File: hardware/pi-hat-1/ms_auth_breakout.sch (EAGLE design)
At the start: 28 parts, among them IC1 ULN2003AD, J11 BUCK_MODULEHORIZONTAL, J9 POWER_JACKPTH_LOCK, Q1 DMN3023L, Q2 DMN3023L, Q3 DMN3023L, Q4 DMN3023L

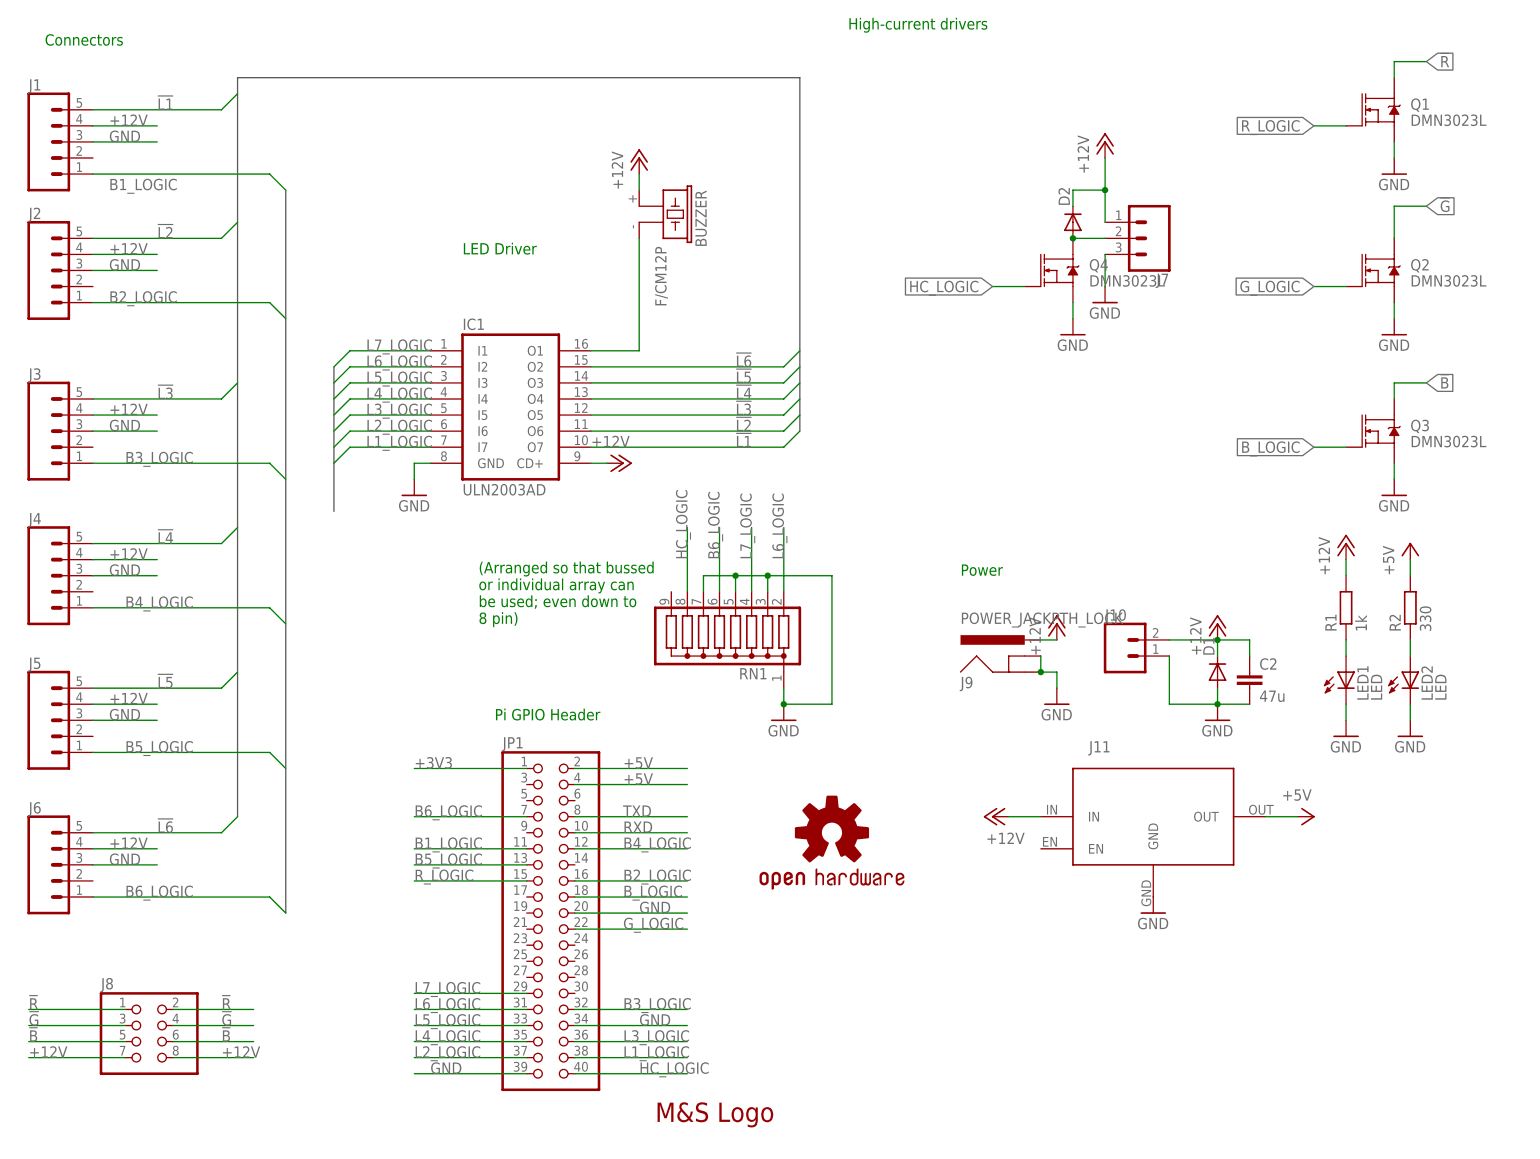
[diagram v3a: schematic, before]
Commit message: Rework board to add two relays.
Also remove buzzer, change LED connector, and standardize on smaller
freewheel diodes.  Not quire ready for 0.4 cut; needs airwires routed
for relays with solder jumpers.
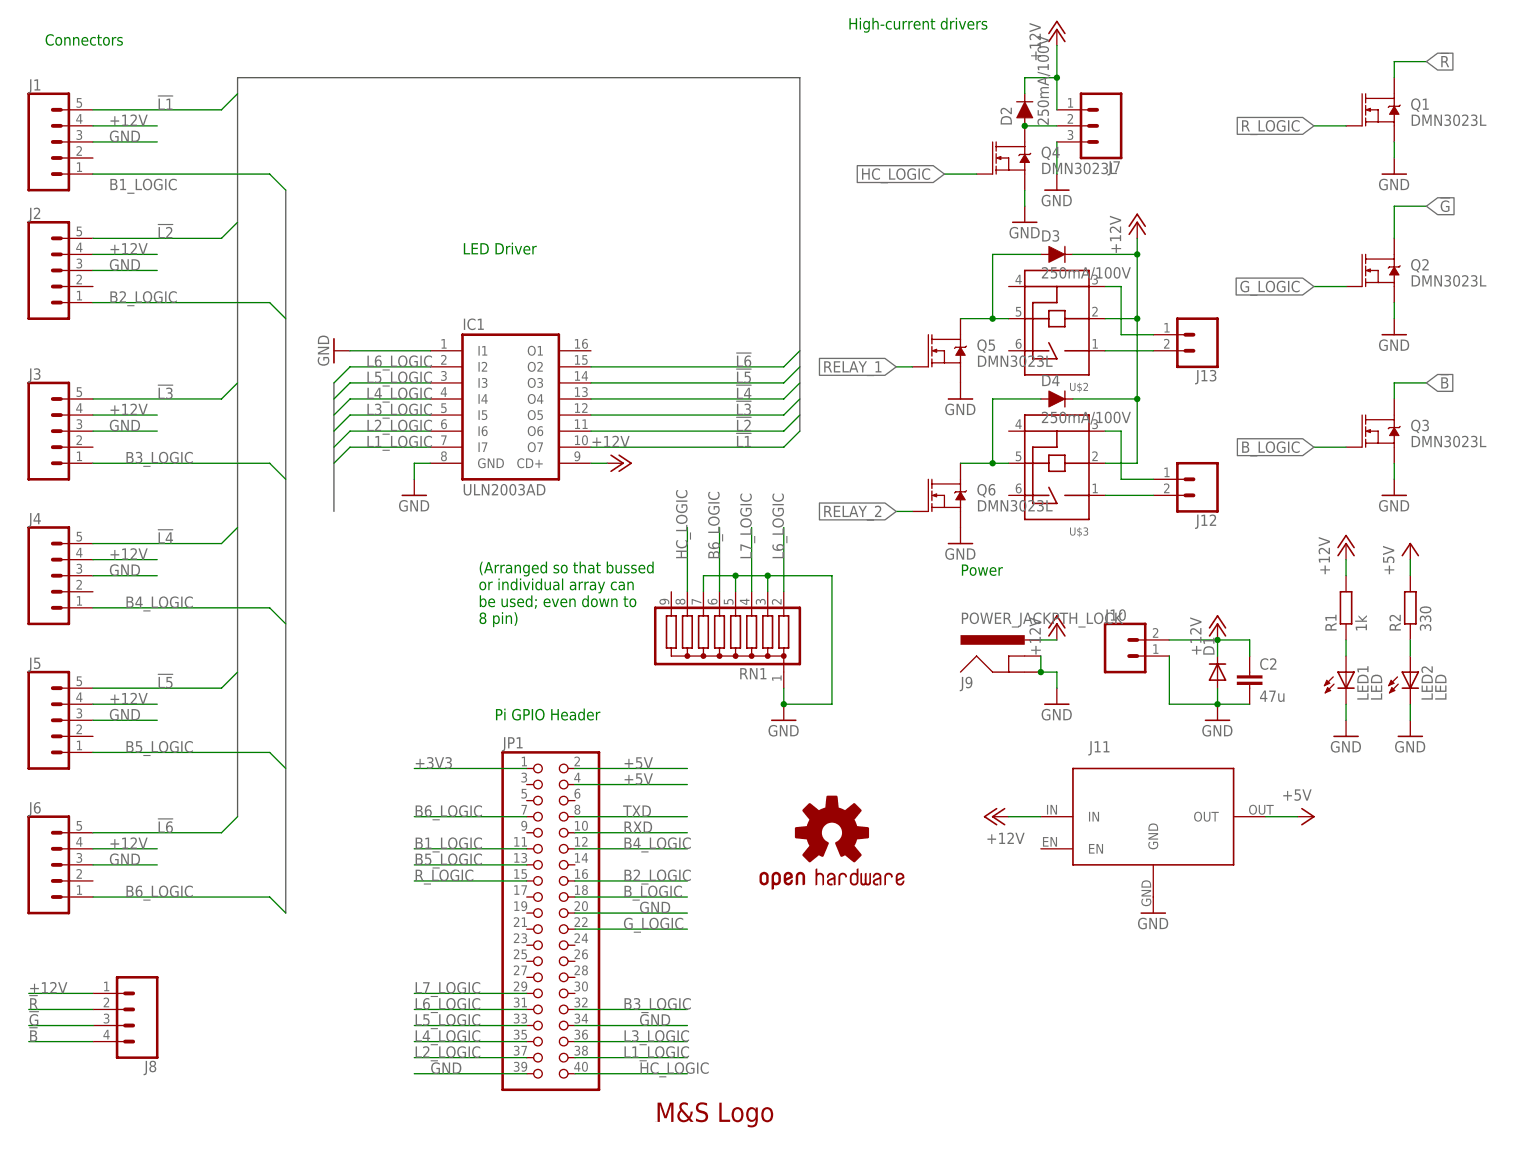
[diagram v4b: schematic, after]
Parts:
- removed BUZZER: F/CM12P, buzzer:F/CM12P
- added D3, D4: 250mA/100V, SparkFun-DiscreteSemi:DIODE-BAS16J
- added J12, J13: (no value), SparkFun-Connectors:CONN_02POLAR_LOCK
- added Q5, Q6: DMN3023L, SparkFun-DiscreteSemi:MOSFET-NCH-AO3404A
- added U$2, U$3: HFD23_SPDT, hfd23:HFD23_SPDT
- D2: value (none) -> 250mA/100V; device diode:DIODE-DO-214AC -> SparkFun-DiscreteSemi:DIODE-BAS16J
- J8: device pinhead:PINHD-2X4 -> SparkFun-Connectors:CONN_04POLAR_LOCK
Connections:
- removed net N$13: BUZZER.2, IC1.O1
- new net N$10: J13.1, U$2.3
- new net N$12: J12.1, U$3.3
- new net N$14: J12.2, U$3.1
- new net N$2: D4.A, Q6.D, U$3.5
- new net N$5: D3.A, Q5.D, U$2.5
- new net N$9: J13.2, U$2.1
- new net RELAY_1: Q5.G
- new net RELAY_2: Q6.G
- net !B: now also J8.4; no longer J8.5, J8.6
- net !G: no longer J8.4
- net !R: no longer J8.1
- net +12V: now also D3.C, D4.C, J8.1, U$2.2, U$3.2; no longer BUZZER.1, J8.7, J8.8
- net GND: now also IC1.I1, Q5.S, Q6.S
- net L7_LOGIC: no longer IC1.I1
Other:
- moved on the sheet: J7, Q4

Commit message: pi-hat-1 v0.4 as-ordered
(Forgot to route the relay connections though.)
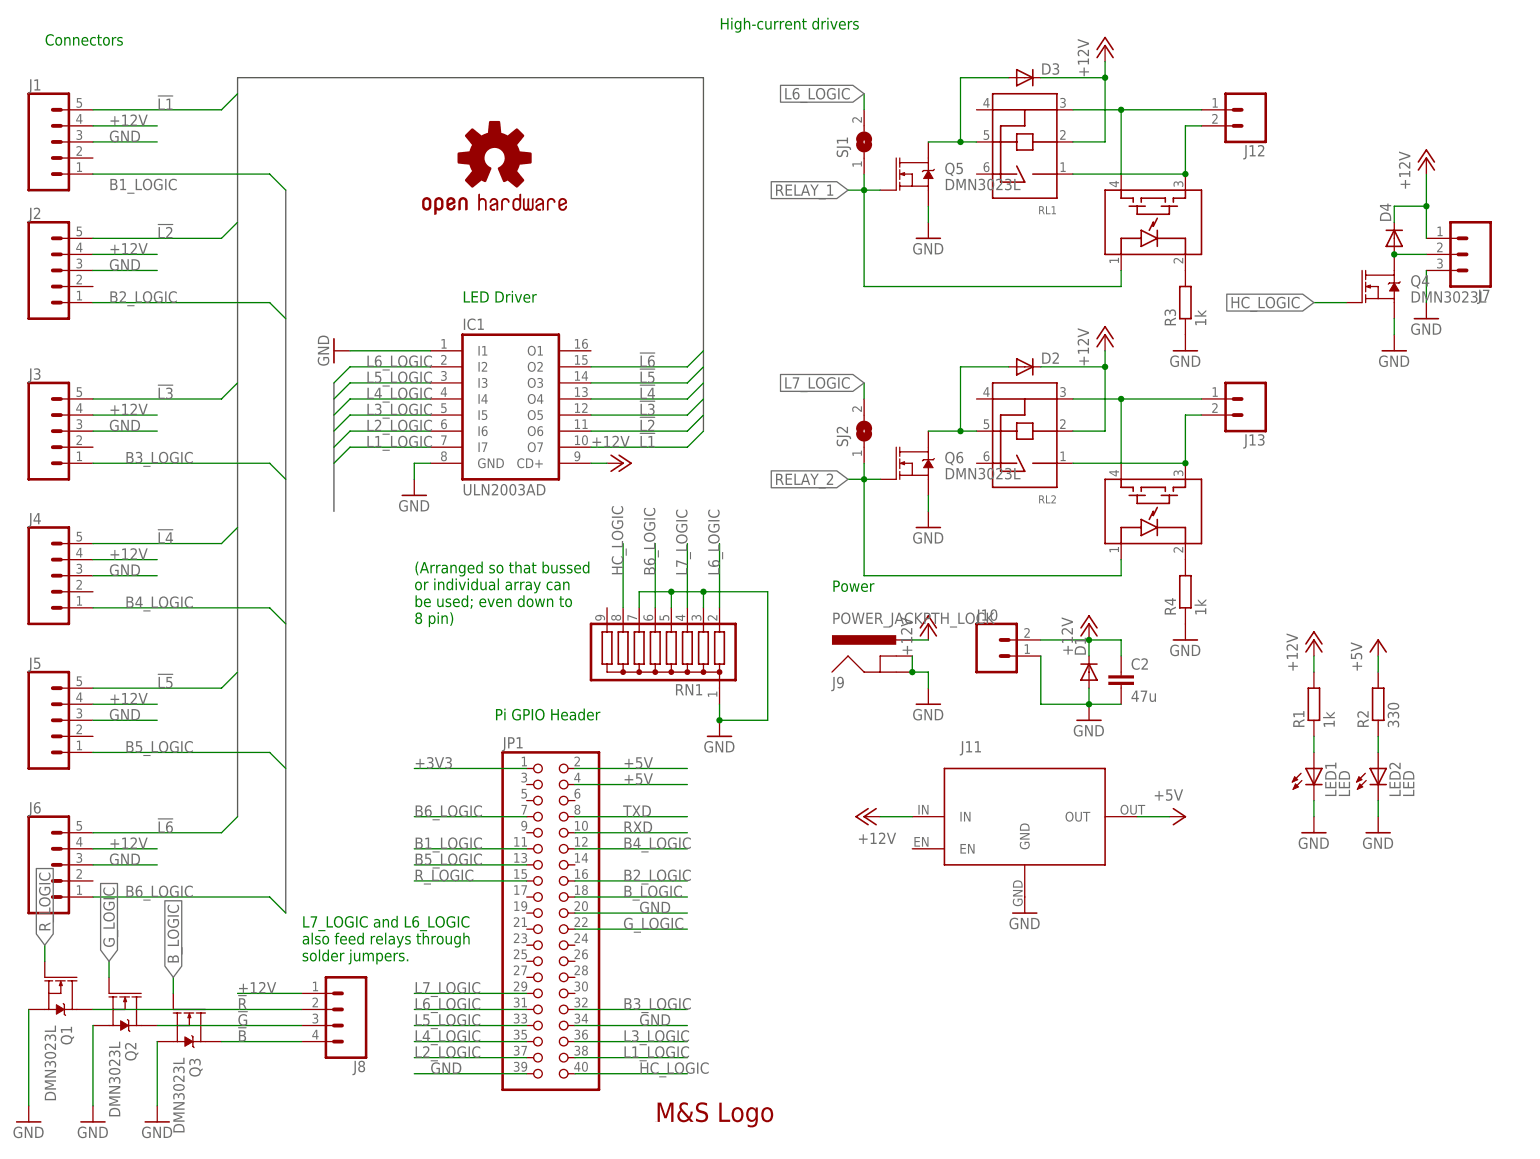
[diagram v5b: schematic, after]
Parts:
- removed U$2, U$3: HFD23_SPDT, hfd23:HFD23_SPDT
- added IC3, IC4: CPC1017, cpc1017:CPC1017
- added R3, R4: 1k, Tim-Pretty:R-EU_R0805
- added RL1, RL2: HFD23_SPDT, hfd23:HFD23_SPDT
- added SJ1, SJ2: (no value), jumper:SJ
- D2, D3, D4: value 250mA/100V -> (none); device SparkFun-DiscreteSemi:DIODE-BAS16J -> diode:DIODE-DO-214AC
- R1, R2: device Tim-Pretty:R-EU_R0603 -> Tim-Pretty:R-EU_R0805
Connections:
- removed net N$14: J12.2, U$3.1
- new net N$13: IC4.2, R4.2
- new net N$6: IC3.3, J12.2, RL1.1
- new net N$8: IC3.2, R3.2
- net +12V: now also RL1.2, RL2.2; no longer U$2.2, U$3.2
- net GND: now also R3.1, R4.1
- net L6_LOGIC: now also SJ1.2
- net L7_LOGIC: now also SJ2.2
- net N$10: now also IC3.4, J12.1, RL1.3; no longer J13.1, U$2.3
- net N$12: now also IC4.4, J13.1, RL2.3; no longer J12.1, U$3.3
- net N$2: now also D2.A, RL2.5; no longer D4.A, U$3.5
- net N$4: now also D4.A; no longer D2.A
- net N$5: now also RL1.5; no longer U$2.5
- net N$9: now also IC4.3, RL2.1; no longer U$2.1
- net RELAY_1: now also IC3.1, SJ1.1
- net RELAY_2: now also IC4.1, SJ2.1
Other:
- note added: "L7_LOGIC and L6_LOGIC also feed relays through solder jumpers."
- moved on the sheet: C2, D1, J10, J11, J12, J13, J7, J8, J9, LED1, LED2, Q1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

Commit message: Authboard change for v1.0
- Remove SOP-4 optos (most test boards we assembled with relays)
- Remove J6 (most test boards for laser need 3 outputs)
- Swap SIP resistor for 4x discrete (easier to mass-produce without it)
- Improve silkscreen around polarity and buck module
- Add MPN/MFN to parts on board.  (Should this go in schematic?)
- Change J5 to support a 3-position switch, intended for marking
  ready/needs-maintenance/down
- Leave some room for an OSH Cert number :)
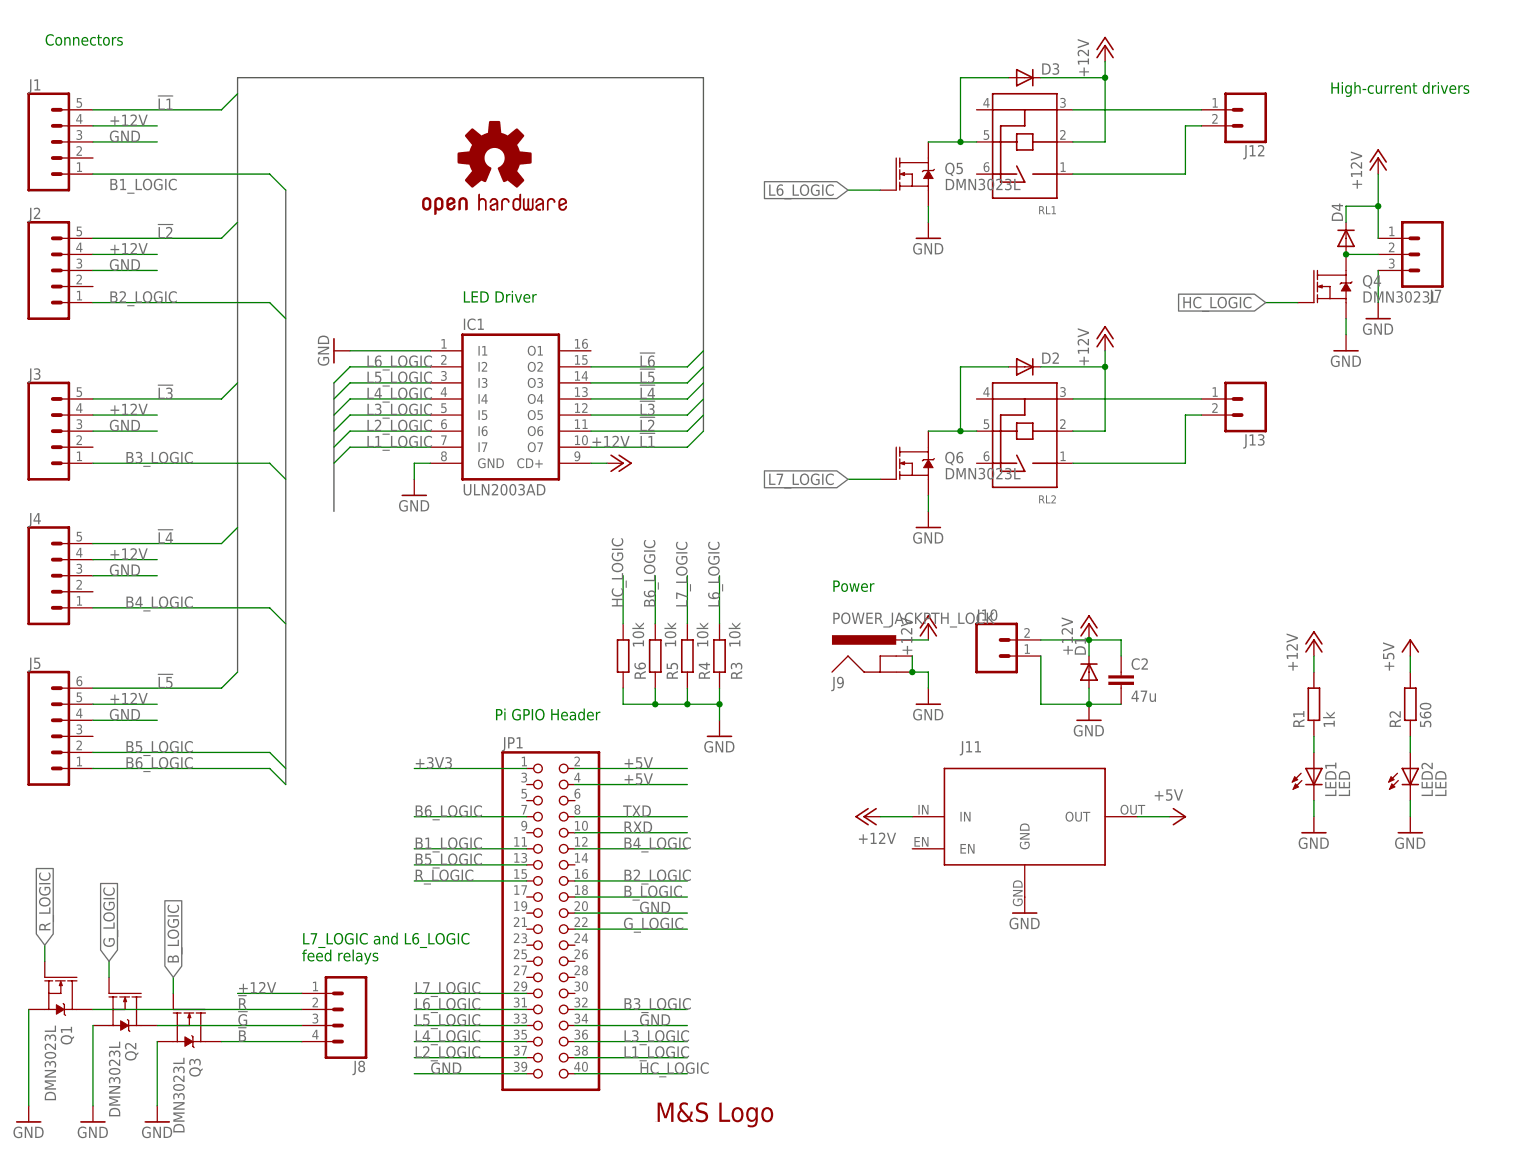
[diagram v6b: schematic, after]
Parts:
- removed IC3, IC4: CPC1017, cpc1017:CPC1017
- removed J6: (no value), SparkFun-Connectors:CONN_05POLAR_LOCK
- removed RN1: (no value), resistor-sil:G08R
- removed SJ1, SJ2: (no value), jumper:SJ
- added R5, R6: 10k, Tim-Pretty:R-EU_R0805
- J5: device SparkFun-Connectors:CONN_05POLAR_LOCK -> SparkFun-Connectors:CONN_06POLAR_LOCK
- R2: value 330 -> 560
- R3, R4: value 1k -> 10k
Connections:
- removed net N$13: IC4.2, R4.2
- removed net N$8: IC3.2, R3.2
- removed net RELAY_1: IC3.1, Q5.G, SJ1.1
- removed net RELAY_2: IC4.1, Q6.G, SJ2.1
- net !L5: now also J5.6; no longer J5.5
- net !L6: no longer J6.5
- net +12V: now also J5.5; no longer J5.4, J6.4
- net B5_LOGIC: now also J5.2; no longer J5.1
- net B6_LOGIC: now also J5.1, R5.2; no longer J6.1, RN1.6
- net GND: now also J5.4, R5.1, R6.1; no longer J5.3, J6.3, RN1.1, RN1.3, RN1.5, RN1.7
- net HC_LOGIC: now also R6.2; no longer RN1.8
- net L6_LOGIC: now also Q5.G, R3.2; no longer RN1.2, SJ1.2
- net L7_LOGIC: now also Q6.G, R4.2; no longer RN1.4, SJ2.2
- net N$10: no longer IC3.4
- net N$12: no longer IC4.4
- net N$6: no longer IC3.3
- net N$9: no longer IC4.3
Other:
- note added: "L7_LOGIC and L6_LOGIC feed relays"
- note removed: "(Arranged so that bussed or individual array can be used; even down to 8 pin)"
- note removed: "L7_LOGIC and L6_LOGIC also feed relays through solder jumpers."
- moved on the sheet: D4, J7, LED2, Q4, R2, R3, R4
